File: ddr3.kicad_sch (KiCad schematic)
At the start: 20 parts, among them U7 MT41K128M16JT-125_K

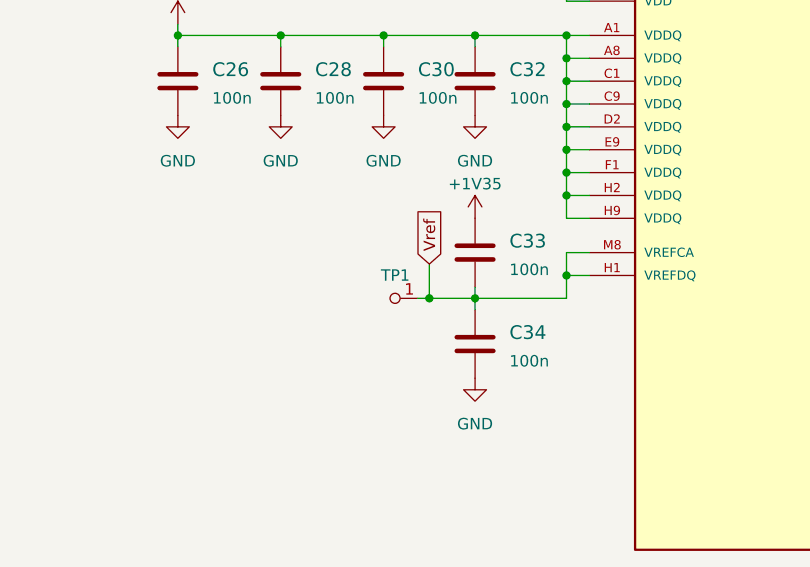
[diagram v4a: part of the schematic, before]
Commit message: Made a connection between DDR3 and fpga on the schematic
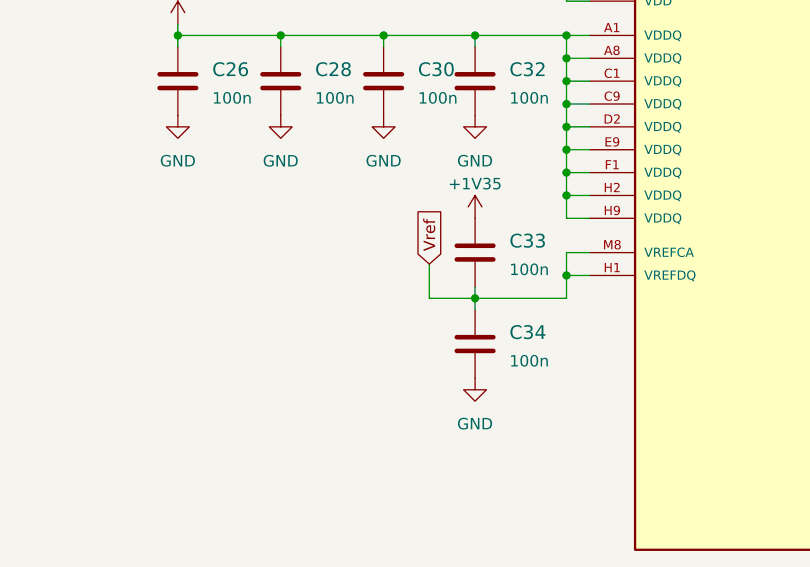
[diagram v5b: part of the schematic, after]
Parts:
- removed TP1: TP, antmicro-footprints:TP-R-1.5, symbol antmicroTestPoints:TP
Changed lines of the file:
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@@
   (junction (at 163.83 46.99) (diameter 0) (color 0 0 0 0)
   )
-  (junction (at 191.77 100.33) (diameter 0) (color 0 0 0 0)
-  )
   (junction (at 76.2 160.02) (diameter 0) (color 0 0 0 0)
   )
@@
   )
   (wire (pts (xy 76.2 138.43) (xy 76.2 135.89))
-    (stroke (width 0) (type default) (color 0 0 0 0))
-  )
-  (wire (pts (xy 190.5 100.33) (xy 191.77 100.33))
     (stroke (width 0) (type default) (color 0 0 0 0))
   )
@@
       (effects (font (size 1.27 1.27)) hide)
     )
-    (pin "1")
-  )
-  (symbol (lib_id "antmicroTestPoints:TP") (at 187.96 100.33 270) (unit 1)
-    (in_bom yes) (on_board yes) (fields_autoplaced)
-    (property "Reference" "TP1" (id 0) (at 187.9981 97.79 90))
-    (property "Value" "TP" (id 1) (at 187.96 100.33 0)
-      (effects (font (size 1.27 1.27)) hide)
-    )
-    (property "Footprint" "antmicro-footprints:TP-R-1.5" (id 2) (at 187.96 100.33 0)
-      (effects (font (size 1.27 1.27)) hide)
-    )
-    (property "Datasheet" "" (id 3) (at 187.96 100.33 0)
-      (effects (font (size 1.27 1.27)) hide)
-    )

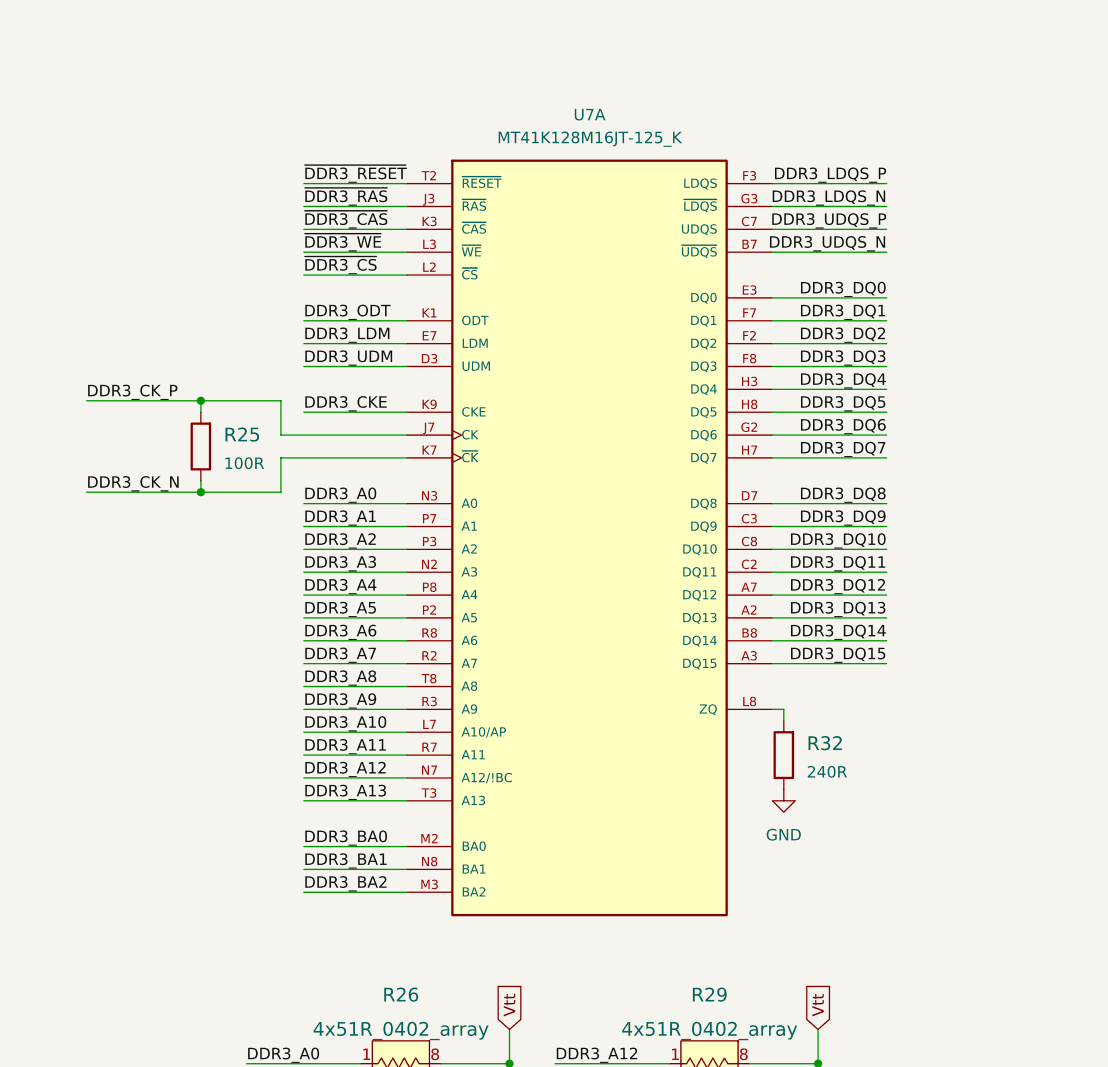
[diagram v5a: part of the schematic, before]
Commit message: Fixed net labels
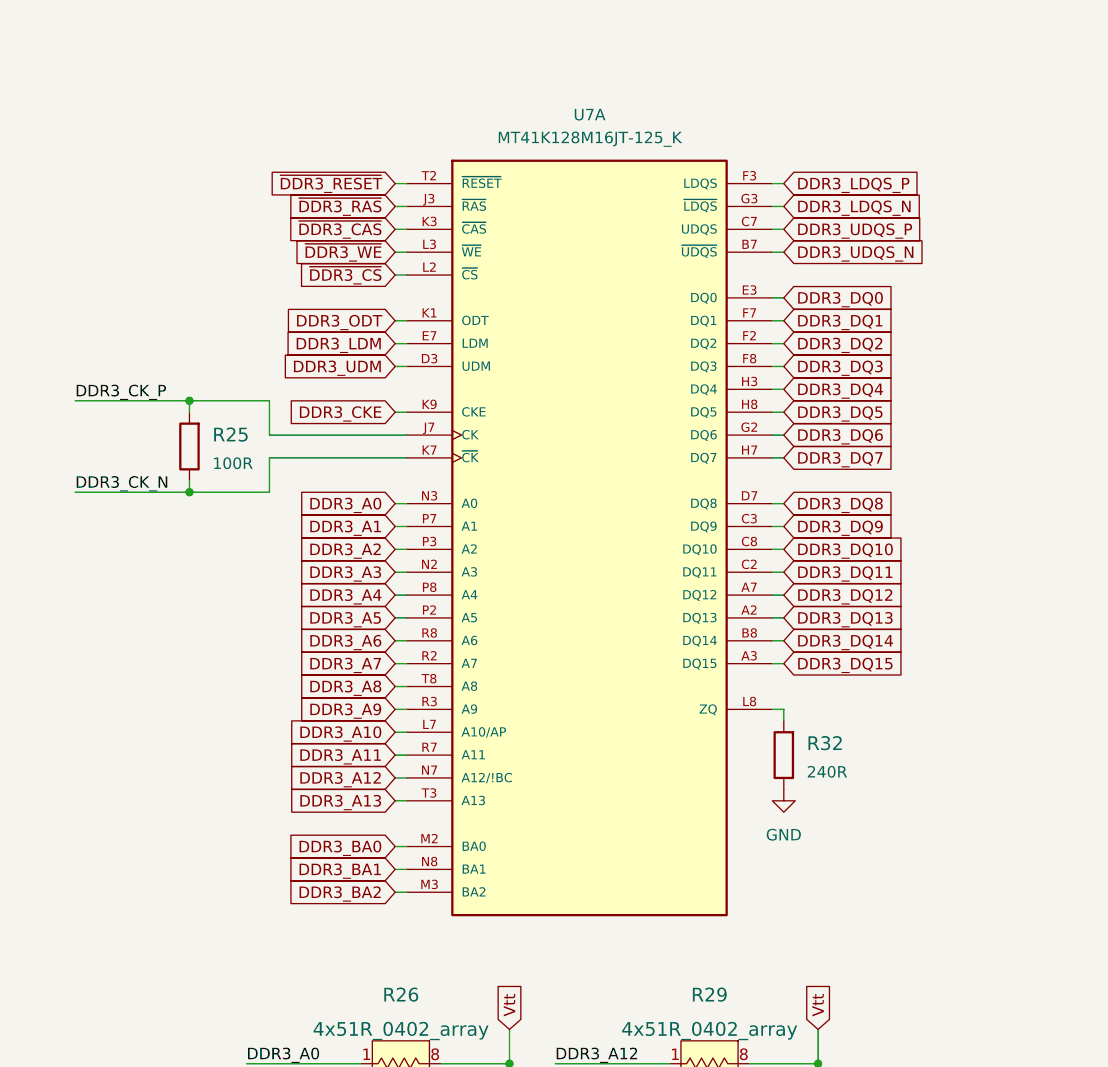
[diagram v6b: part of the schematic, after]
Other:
- moved on the sheet: R25

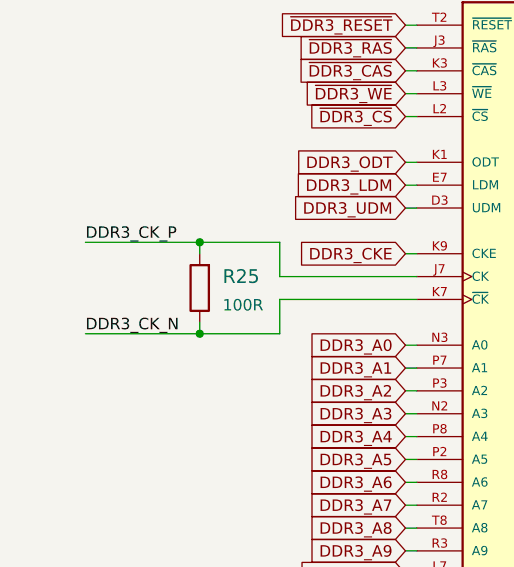
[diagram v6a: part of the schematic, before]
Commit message: Connected soft MIPI CSI to FPGA
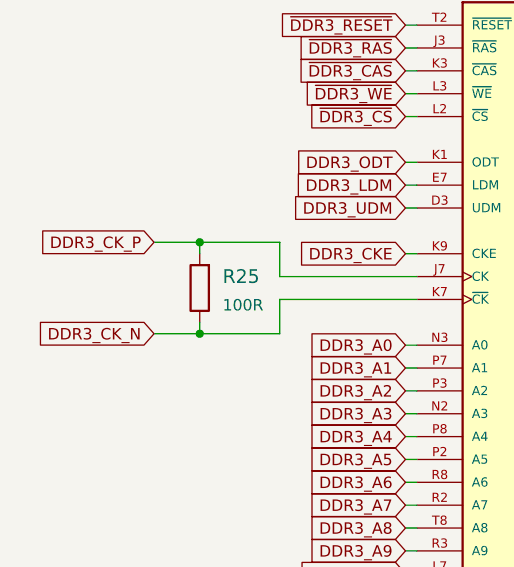
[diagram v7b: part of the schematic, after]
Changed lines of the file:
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@@
   (junction (at 252.73 59.69) (diameter 0) (color 0 0 0 0)
   )
+  (junction (at 76.2 154.94) (diameter 0) (color 0 0 0 0)
+  )
+  (junction (at 207.01 54.61) (diameter 0) (color 0 0 0 0)
+  )
+  (junction (at 40.64 59.69) (diameter 0) (color 0 0 0 0)
+  )
+  (junction (at 252.73 74.93) (diameter 0) (color 0 0 0 0)
+  )
+  (junction (at 110.49 133.35) (diameter 0) (color 0 0 0 0)
+  )
+  (junction (at 110.49 157.48) (diameter 0) (color 0 0 0 0)
+  )
+  (junction (at 207.01 59.69) (diameter 0) (color 0 0 0 0)
+  )
+  (junction (at 110.49 138.43) (diameter 0) (color 0 0 0 0)
+  )
+  (junction (at 196.85 46.99) (diameter 0) (color 0 0 0 0)
+  )
+  (junction (at 76.2 176.53) (diameter 0) (color 0 0 0 0)
+  )
+  (junction (at 207.01 46.99) (diameter 0) (color 0 0 0 0)
+  )
+  (junction (at 110.49 154.94) (diameter 0) (color 0 0 0 0)
+  )
+  (junction (at 252.73 91.44) (diameter 0) (color 0 0 0 0)
+  )
+  (junction (at 207.01 76.2) (diameter 0) (color 0 0 0 0)
+  )
+  (junction (at 110.49 160.02) (diameter 0) (color 0 0 0 0)
+  )
+  (junction (at 207.01 57.15) (diameter 0) (color 0 0 0 0)
+  )
+  (junction (at 252.73 99.06) (diameter 0) (color 0 0 0 0)
+  )
+  (junction (at 207.01 78.74) (diameter 0) (color 0 0 0 0)
+  )
   (junction (at 40.64 69.85) (diameter 0) (color 0 0 0 0)
   )
-  (junction (at 76.2 154.94) (diameter 0) (color 0 0 0 0)
-  )
-  (junction (at 207.01 54.61) (diameter 0) (color 0 0 0 0)
-  )
-  (junction (at 252.73 74.93) (diameter 0) (color 0 0 0 0)
-  )
-  (junction (at 110.49 133.35) (diameter 0) (color 0 0 0 0)
-  )
-  (junction (at 110.49 157.48) (diameter 0) (color 0 0 0 0)
-  )
-  (junction (at 207.01 59.69) (diameter 0) (color 0 0 0 0)
-  )
-  (junction (at 110.49 138.43) (diameter 0) (color 0 0 0 0)
-  )
-  (junction (at 196.85 46.99) (diameter 0) (color 0 0 0 0)
-  )
-  (junction (at 76.2 176.53) (diameter 0) (color 0 0 0 0)
-  )
-  (junction (at 207.01 46.99) (diameter 0) (color 0 0 0 0)
-  )
-  (junction (at 110.49 154.94) (diameter 0) (color 0 0 0 0)
-  )
-  (junction (at 252.73 91.44) (diameter 0) (color 0 0 0 0)
-  )
-  (junction (at 207.01 76.2) (diameter 0) (color 0 0 0 0)
-  )
-  (junction (at 110.49 160.02) (diameter 0) (color 0 0 0 0)
-  )
-  (junction (at 207.01 57.15) (diameter 0) (color 0 0 0 0)
-  )
-  (junction (at 252.73 99.06) (diameter 0) (color 0 0 0 0)
-  )
-  (junction (at 207.01 78.74) (diameter 0) (color 0 0 0 0)
-  )
   (junction (at 252.73 64.77) (diameter 0) (color 0 0 0 0)
   )
@@
   (junction (at 196.85 100.33) (diameter 0) (color 0 0 0 0)
   )
-  (junction (at 40.64 59.69) (diameter 0) (color 0 0 0 0)
-  )
   (junction (at 110.49 179.07) (diameter 0) (color 0 0 0 0)
   )
@@
     (stroke (width 0) (type default) (color 0 0 0 0))
   )
+  (wire (pts (xy 35.56 59.69) (xy 40.64 59.69))
+    (stroke (width 0) (type default) (color 0 0 0 0))
+  )
   (wire (pts (xy 207.01 49.53) (xy 207.01 46.99))
     (stroke (width 0) (type default) (color 0 0 0 0))
@@
     (stroke (width 0) (type default) (color 0 0 0 0))
   )
-  (wire (pts (xy 27.94 59.69) (xy 40.64 59.69))
-    (stroke (width 0) (type default) (color 0 0 0 0))
-  )
   (wire (pts (xy 250.19 52.07) (xy 252.73 52.07))
     (stroke (width 0) (type default) (color 0 0 0 0))
@@
     (stroke (width 0) (type default) (color 0 0 0 0))
   )
-  (wire (pts (xy 27.94 69.85) (xy 40.64 69.85))
+  (wire (pts (xy 35.56 69.85) (xy 40.64 69.85))
     (stroke (width 0) (type default) (color 0 0 0 0))
   )
@@
     (effects (font (size 1.27 1.27)) (justify left bottom))
   )
-  (label "DDR3_CK_N" (at 27.94 69.85 0)
-    (effects (font (size 1.27 1.27)) (justify left bottom))
-  )
   (label "DDR3_A7" (at 46.99 162.56 0)
     (effects (font (size 1.27 1.27)) (justify left bottom))
@@
   )
   (label "DDR3_ODT" (at 81.28 179.07 0)
-    (effects (font (size 1.27 1.27)) (justify left bottom))
-  )
-  (label "DDR3_CK_P" (at 27.94 59.69 0)
     (effects (font (size 1.27 1.27)) (justify left bottom))
   )
@@
     )
   )
+  (global_label "DDR3_CK_N" (shape input) (at 35.56 69.85 180) (fields_autoplaced)
+    (effects (font (size 1.27 1.27)) (justify right))
+    (property "Intersheet References" "${INTERSHEET_REFS}" (id 0) (at 22.3217 69.7706 0)
+      (effects (font (size 1.27 1.27)) (justify right) hide)
+    )
+  )
   (global_label "Vtt" (shape input) (at 110.49 151.13 90) (fields_autoplaced)
     (effects (font (size 1.27 1.27)) (justify left))
@@
       (effects (font (size 1.27 1.27)) (justify right) hide)
     )
+  )
+  (global_label "DDR3_CK_P" (shape input) (at 35.56 59.69 180) (fields_autoplaced)
+    (effects (font (size 1.27 1.27)) (justify right))
+    (property "Intersheet References" "${INTERSHEET_REFS}" (id 0) (at 22.3821 59.6106 0)
+      (effects (font (size 1.27 1.27)) (justify right) hide)
+    )

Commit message: Made PCB mockup
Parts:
- renumbered C25 to C33, C26 to C34, C27 to C35, C28 to C36, C29 to C37, C30 to C38, C31 to C39, C32 to C40, C33 to C41, C34 to C42, R25 to R47, R26 to R48, R27 to R49, R28 to R50, R29 to R51, R30 to R52, R31 to R53, R32 to R54, U7 to U8
